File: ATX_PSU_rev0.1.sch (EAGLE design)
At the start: 60 parts, among them J1 ATX24RH, U1 INA169, U2 INA169, U3 INA169, U4 INA169, U5 INA169

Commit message: added microcontroller
made some connections to microcontroller.
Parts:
- added C6: 100nF, resistor:C-USC1206
- added J25: AVR_SPI_PROG_3X22X3_LOCK, SparkFun-Connectors:AVR_SPI_PROG_3X22X3_LOCK
- added R16: 10K, resistor:R-US_R1206
- added U7: (no value), Seeed-IC:MCU-ATMEGA168PA-MU(QFN32)
- added Y1: (no value), SparkFun-Clocks:RESONATORSMD-3.2X1.3
- C1, C2, C3, C4, C5: value (none) -> 0.1uF
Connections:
- removed net N$10: R14.1
- removed net N$12: R13.1
- removed net N$13: R12.1
- removed net N$14: R11.1
- removed net N$9: R15.1
- new net LED0: R11.1, U7.PD0(RXD/PCINT16
- new net LED1: R12.1, U7.PD1(TXD/PCINT17
- new net LED2: R13.1, U7.PD2(INT0/PCINT18)
- new net LED3: R14.1, U7.PD3(INT1/OC2B/PCINT19)
- new net LED4: R15.1, U7.PD4(T0/XCK/PCINT20)
- new net MISO: J25.1, U7.PB4(MISO/PCINT4)
- new net MOSI: J25.4, U7.PB3(MOSI/OC2A/PCINT3)
- new net N$11: U7.PB6(TDSC1/XTAL1/PCINT6), Y1.3
- new net N$8: U7.PB7(TOSC2/XTAL2/PCINT7), Y1.1
- new net RST: J25.5, R16.1, U7.PC6(RESET/PCINT14)
- new net SCK: J25.3, U7.PB5(SCK/PCINT5)
- net 5V_STDBY_PRE: now also C6.1, J25.2, R16.2, U7.AVCC, U7.VCC, U7.VCC@1
- net ECHO_0: now also U7.PC4(ADC4/SDA/PCINT12)
- net ECHO_1: now also U7.PC3(ADC3/PCINT11)
- net ECHO_2: now also U7.PC2(ADC2/PCINT10)
- net ECHO_3: now also U7.PC0(ADC0/PCINT8)
- net ECHO_4: now also U7.PC1(ADC1/PCINT9)
- net GND: now also C6.2, J25.6, U7.GND, U7.GND@1, U7.GND@2, U7.PAD, Y1.2

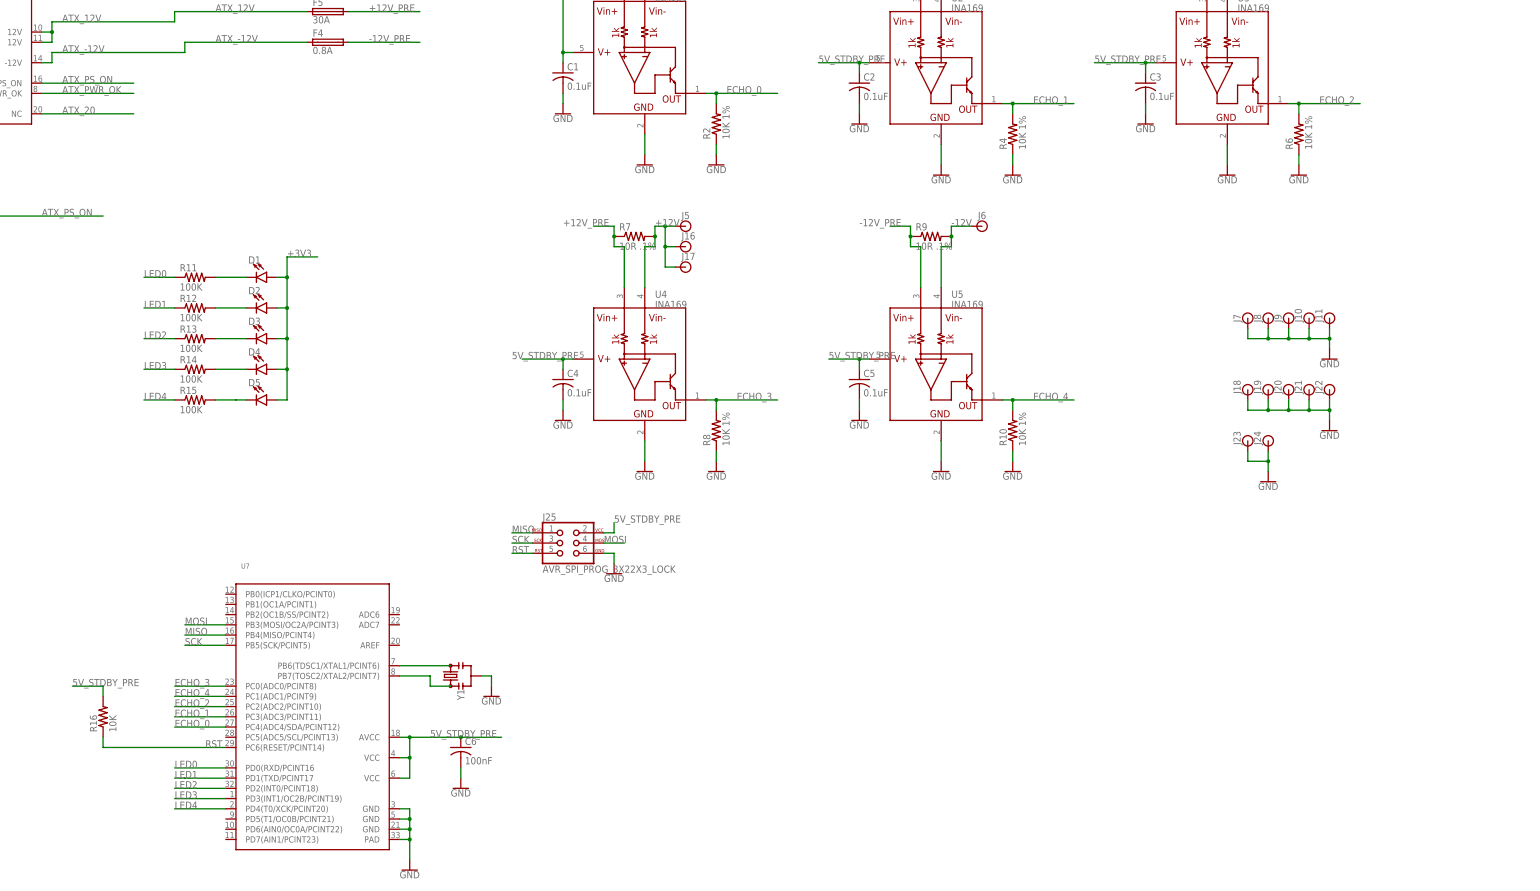
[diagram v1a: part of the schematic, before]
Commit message: added some parts
LCD with I2C backpack and 3 buttons.
I belive routing is finished, but I want to reroute using polygons for large connectors, and figure out how this will be enclosed.
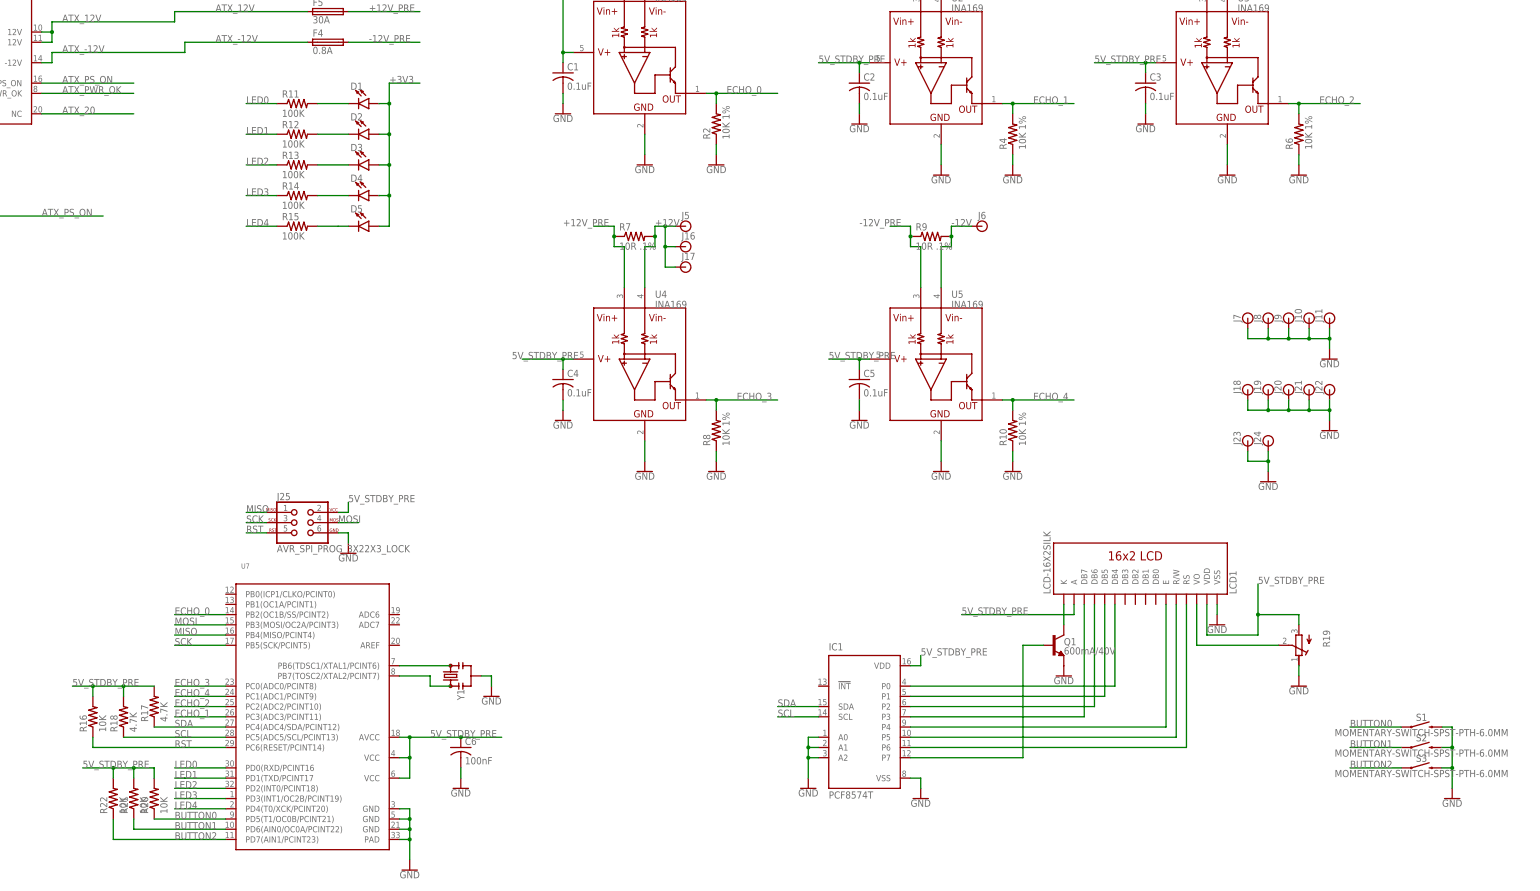
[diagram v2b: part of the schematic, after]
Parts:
- added IC1: PCF8574T, micro-philips:PCF8574T
- added LCD1: LCD-16X2SILK, SparkFun-Displays:LCD-16X2SILK
- added Q1: 600mA/40V, SparkFun-DiscreteSemi:TRANS_NPN-MMBT2222AL
- added R17, R18: 4.7K, resistor:R-US_R1206
- added R19: (no value), resistor:R-TRIMM3314G
- added R20, R21, R22: 10K, resistor:R-US_R1206
- added S1, S2, S3: MOMENTARY-SWITCH-SPST-PTH-6.0MM, SparkFun-Switches:MOMENTARY-SWITCH-SPST-PTH-6.0MM
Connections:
- new net BUTTON0: R20.1, S1.1, U7.PD5(T1/OC0B/PCINT21)
- new net BUTTON1: R21.1, S2.1, U7.PD6(AIN0/OC0A/PCINT22)
- new net BUTTON2: R22.1, S3.1, U7.PD7(AIN1/PCINT23)
- new net N$10: IC1.P3, LCD1.DB7
- new net N$12: IC1.P4, LCD1.E
- new net N$13: IC1.P5, LCD1.R/W
- new net N$14: IC1.P6, LCD1.RS
- new net N$15: IC1.P7, Q1.B
- new net N$16: LCD1.K, Q1.C
- new net N$18: LCD1.VO, R19.S
- new net N$3: IC1.P0, LCD1.DB4
- new net N$7: IC1.P1, LCD1.DB5
- new net N$9: IC1.P2, LCD1.DB6
- new net SCL: IC1.SCL, R18.1, U7.PC5(ADC5/SCL/PCINT13)
- new net SDA: IC1.SDA, R17.1, U7.PC4(ADC4/SDA/PCINT12)
- net 5V_STDBY_PRE: now also IC1.VDD, LCD1.A, LCD1.VDD, R17.2, R18.2, R19.A, R20.2, R21.2, R22.2
- net ECHO_0: now also U7.PB2(OC1B/SS/PCINT2); no longer U7.PC4(ADC4/SDA/PCINT12)
- net GND: now also IC1.A0, IC1.A1, IC1.A2, IC1.VSS, LCD1.VSS, Q1.E, R19.E, S1.2, S2.2, S3.2
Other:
- moved on the sheet: D1, D2, D3, D4, D5, J25, R11, R12, R13, R14, R15, R16
